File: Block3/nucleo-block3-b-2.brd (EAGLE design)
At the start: 100.3 x 80 mm, 91 parts, among them IC1 TL331, J4 MODJACK6P6C-MJ3245-66-0CONN_M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, J5 MODJACK6P6C-MJ3245-66-0CONN_M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, Q1 NPN-23, Q2 BSS123, Q3 BSS84, U1 TC4428, U2 TC4428, U3 TC4428

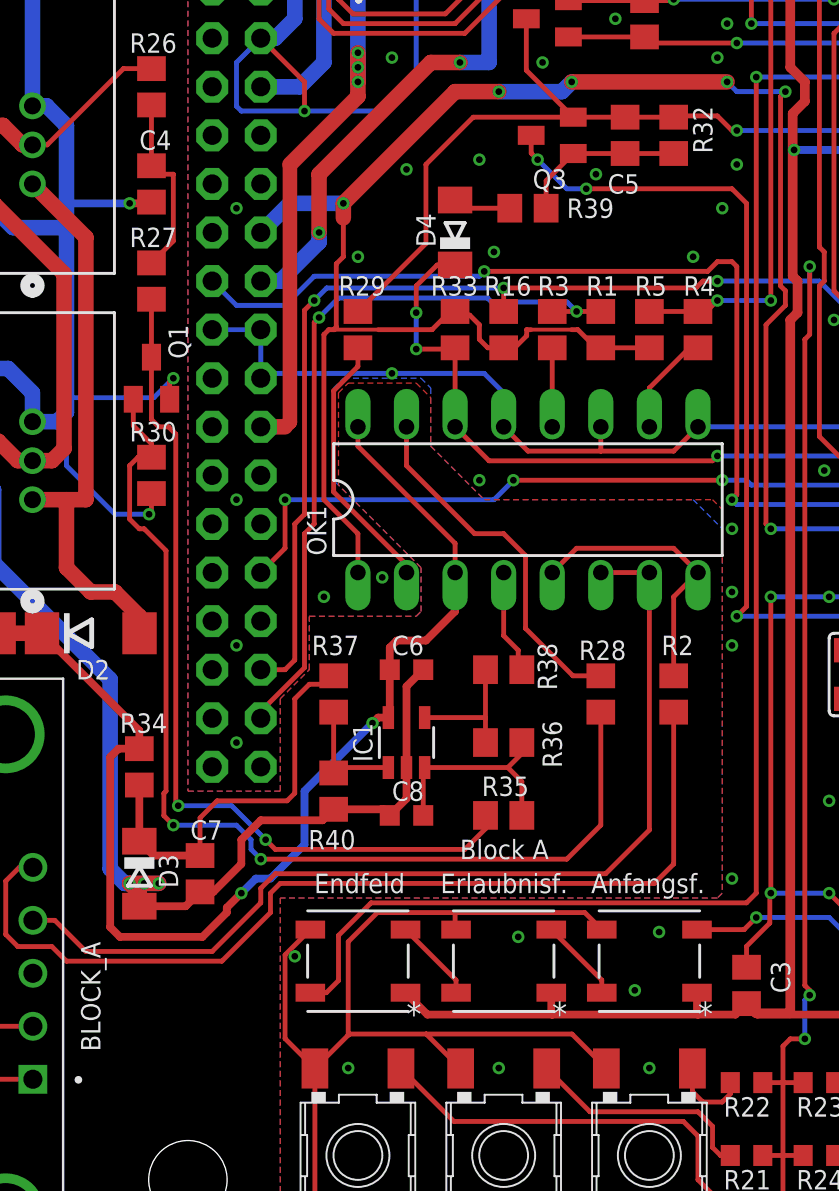
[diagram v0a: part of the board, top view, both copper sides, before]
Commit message: - adds a small TH pin "alignment hole" to the lib - fixes the DB-9 connector's pin order - updates the loconet-block3 board for rev B.
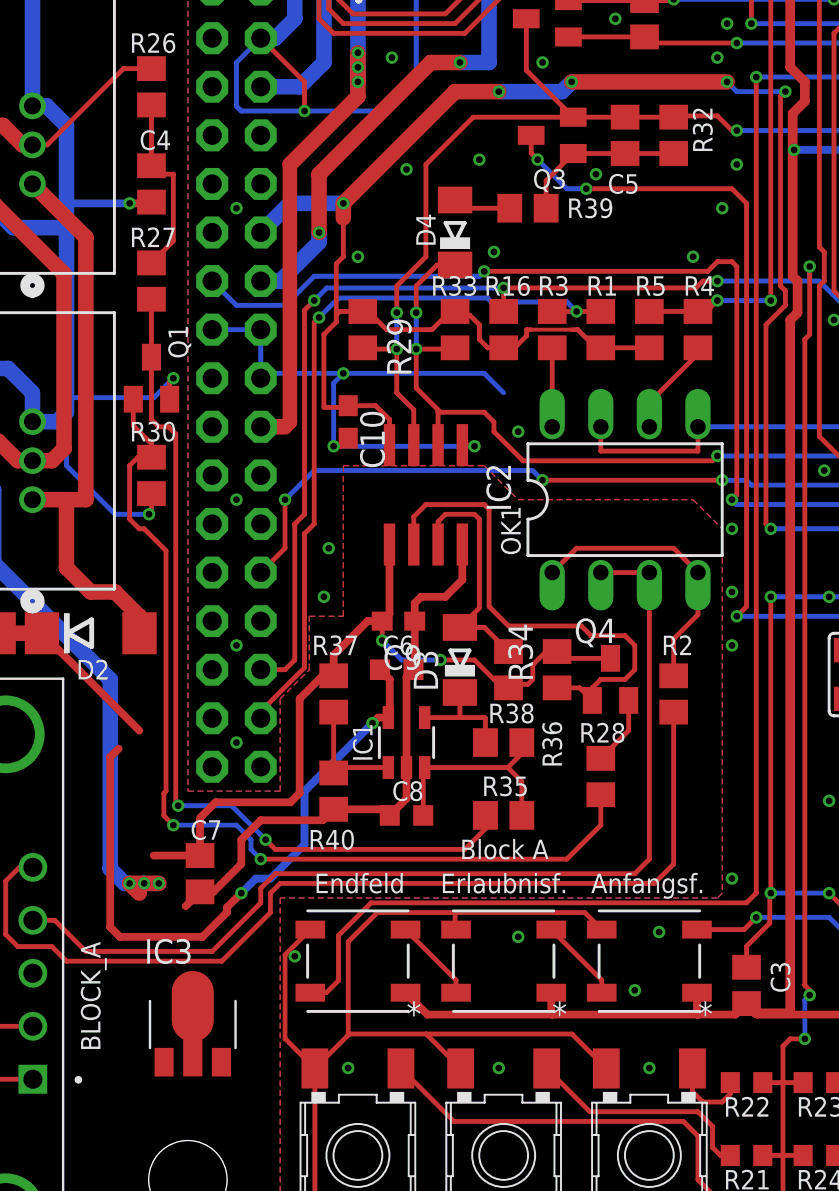
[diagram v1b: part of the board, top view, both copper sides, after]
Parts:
- added C10, C9: (no value), rcl:C0603
- added IC2: ISO7221A, texas:SO-08
- added IC3: 78L05F, linear:SOT89
- added Q4: BSS84, eagleparts:SOT23-PCH
- D3: value 5V1 -> (none); device diode:SOD80C -> diode:MINIMELF
- OK1: value PC847 -> PC827; device optocoupler:DIL16 -> optocoupler:DIL08
- R29: value 200 -> 10k
- R34: value 1k -> 10k
- R38: value 1k5 -> 10k
- moved R34 22.4 mm to (38.4, 31.8), turned to 90 degrees
- moved D3 20.1 mm to (33.3, 32.3), turned to 90 degrees
- moved OK1 5.08 mm to (41.9, 40.6)
- moved R28 4.32 mm to (40.6, 26.2)
- moved C6 0.51 mm to (30.0, 31.8)
- moved R29 0.25 mm to (28.2, 49.5), turned to 270 degrees
- moved R38 0.25 mm to (35.8, 31.8), turned to 270 degrees
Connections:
- removed net N$38: OK1.2, R29.1
- removed net N$39: OK1.4, R38.2
- new net N$20: D3.A, IC2.3, R38.1
- new net N$8: IC2.2, Q4.1, R34.1
- net AGND: now also C9.1, IC2.4, IC3.2, IC3.2@1; no longer D3.A
- net BLKA-RX-: now also OK1.2, OK1.3; no longer OK1.6, OK1.7
- net GND: now also C10.2, IC2.5, OK1.5, OK1.7; no longer OK1.11, OK1.13, OK1.9
- net LN-RX: now also IC2.6; no longer OK1.14
- net LN-TX: now also IC2.7
- net LN5V: now also C9.2, IC2.1, IC3.1, Q4.3, R38.2; no longer D3.C
- net LNPLUS: now also IC3.3; no longer OK1.16, OK1.3, R34.1
- net N$11: now also Q4.2; no longer OK1.15
- net N$31: now also OK1.1, OK1.4; no longer OK1.5, OK1.8
- net N$36: now also D3.C; no longer R38.1
- net N$41: now also OK1.8; no longer OK1.12
- net N$42: now also OK1.6; no longer OK1.10
- net VCC: now also C10.1, IC2.8, R29.1; no longer OK1.1
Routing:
- net N$8: track 0.00 -> 26.0 mm
- net LN5V: track 21.3 -> 43.2 mm, vias 0 -> 2
- net LNPLUS: track 118.6 -> 99.6 mm
- net N$11: track 19.0 -> 3.63 mm
- net N$38: track 13.9 -> 0.00 mm
- net N$20: track 0.00 -> 12.8 mm
- net LN-TX: track 77.6 -> 85.9 mm, vias 3 -> 5
- net GND: track 508.9 -> 515.3 mm, vias 113 -> 115
- net N$39: track 5.47 -> 0.00 mm
- net AGND: track 126.3 -> 131.3 mm
- net LN-TX-B: track 54.8 -> 50.4 mm
- net VCC: track 120.1 -> 116.0 mm
- net LN-RX: track 71.4 -> 74.3 mm
- net N$36: track 7.00 -> 5.78 mm
- net BLKA-RX-: track 52.0 -> 52.9 mm
